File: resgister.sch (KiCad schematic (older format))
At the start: 6 parts, among them U11 74LS245, U12 74LS173, U13 74LS173, U14 74LS245, U15 74LS173, U16 74LS173

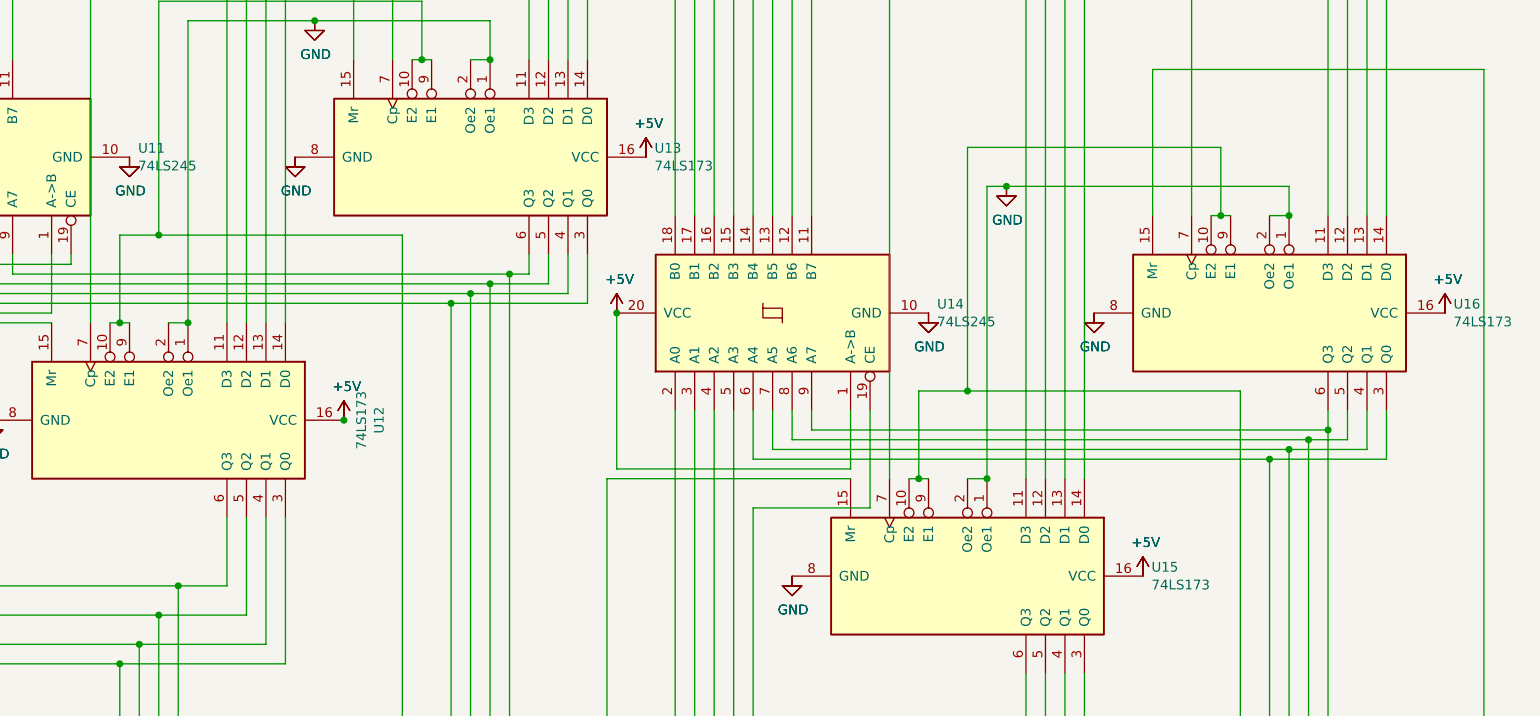
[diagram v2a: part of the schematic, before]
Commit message: Added footprints
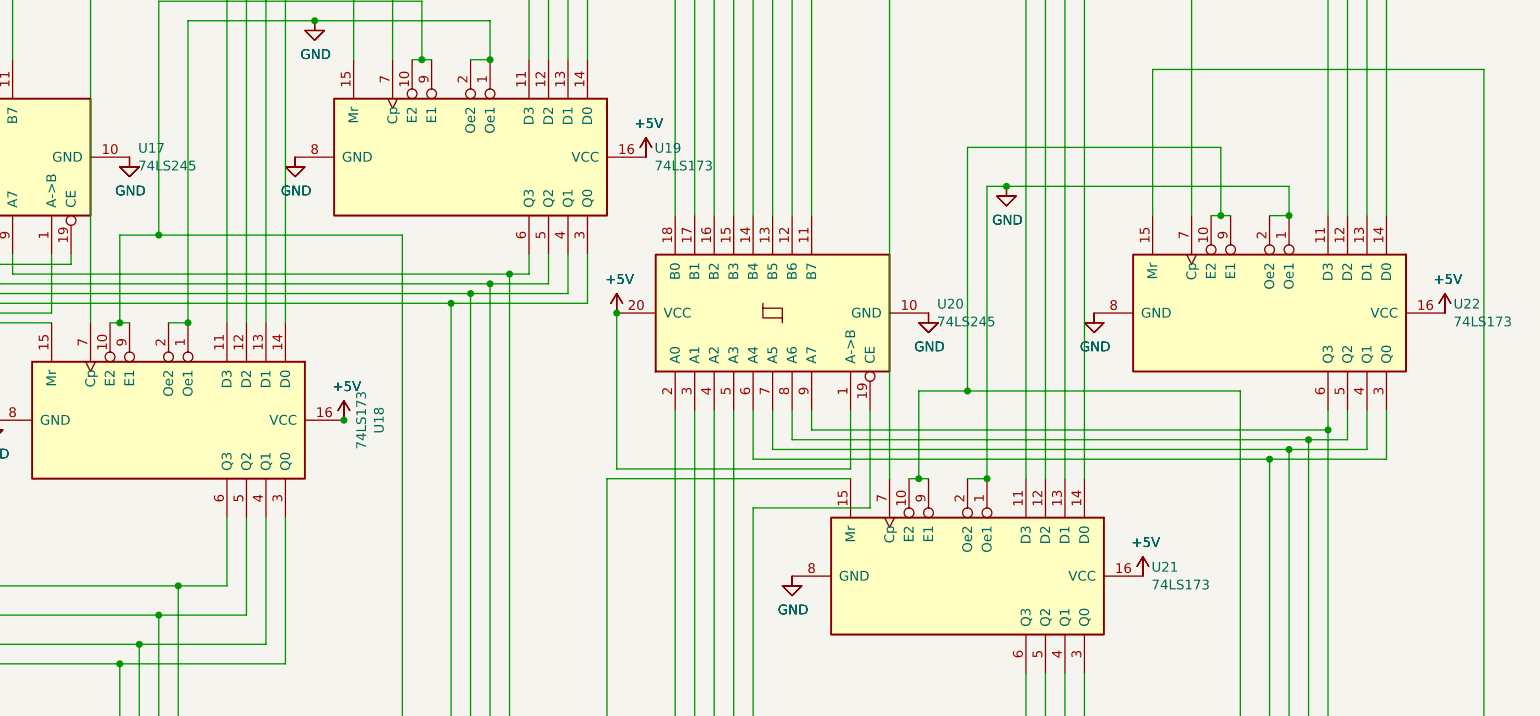
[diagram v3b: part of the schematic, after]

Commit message: Fixed ZIF
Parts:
- U11, U14: symbol 74xx:74LS245 -> 16bitCpu-rescue:74LS245-74xx
- U12, U13, U15, U16: symbol 74xx:74LS173 -> 16bitCpu-rescue:74LS173-74xx
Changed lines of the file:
@@
 	8100 6150 8100 6800
 $Comp
-L power:GND #PWR?
+L 16bitCpu-rescue:GND-power #PWR?
 U 1 1 5F7355A1
 P 7400 4300
@@
 $EndComp
 $Comp
-L power:GND #PWR?
+L 16bitCpu-rescue:GND-power #PWR?
 U 1 1 5F7355A2
 P 8250 4300
@@
 $EndComp
 $Comp
-L power:GND #PWR?
+L 16bitCpu-rescue:GND-power #PWR?
 U 1 1 5F7355A3
 P 6700 5650
@@
 $EndComp
 $Comp
-L power:GND #PWR?
+L 16bitCpu-rescue:GND-power #PWR?
 U 1 1 5F6AAC3B
 P 2600 4850
@@
 $EndComp
 $Comp
-L power:GND #PWR?
+L 16bitCpu-rescue:GND-power #PWR?
 U 1 1 5F6AAC41
 P 3300 3500
@@
 $EndComp
 $Comp
-L power:GND #PWR?
+L 16bitCpu-rescue:GND-power #PWR?
 U 1 1 5F6AAC47
 P 4150 3500
@@
 $EndComp
 $Comp
-L power:+5V #PWR?
+L 16bitCpu-rescue:+5V-power #PWR?
 U 1 1 5F7355A8
 P 4400 4850
@@
 $EndComp
 $Comp
-L power:+5V #PWR?
+L 16bitCpu-rescue:+5V-power #PWR?
 U 1 1 5F7355A9
 P 5800 4300
@@
 $EndComp
 $Comp
-L power:+5V #PWR?
+L 16bitCpu-rescue:+5V-power #PWR?
 U 1 1 5F7355AA
 P 8500 5650
@@
 $EndComp
 $Comp
-L power:+5V #PWR?
+L 16bitCpu-rescue:+5V-power #PWR?
 U 1 1 5F7355AB
 P 10050 4300
@@
 $EndComp
 $Comp
-L power:+5V #PWR?
+L 16bitCpu-rescue:+5V-power #PWR?
 U 1 1 5F7355AC
 P 5950 3500
@@
 Connection ~ 5150 3000
 $Comp
-L power:GND #PWR?
+L 16bitCpu-rescue:GND-power #PWR?
 U 1 1 5F7355AD
 P 4250 2800
@@
 Connection ~ 9250 3800
 $Comp
-L power:GND #PWR?
+L 16bitCpu-rescue:GND-power #PWR?
 U 1 1 5F6AAC87
 P 7800 3650
@@
 	6500 8600 10200 8600
 $Comp
-L 74xx:74LS173 U?
+L 16bitCpu-rescue:74LS173-74xx U?
 U 1 1 5F6AAB55
 P 3500 4850
@@
 $EndComp
 $Comp
-L 74xx:74LS245 U?
+L 16bitCpu-rescue:74LS245-74xx U?
 U 1 1 5F6AAB61
 P 2500 3500
@@
 $EndComp
 $Comp
-L 74xx:74LS173 U?
+L 16bitCpu-rescue:74LS173-74xx U?
 U 1 1 5F73559F
 P 9150 4300
@@
 $EndComp
 $Comp
-L power:GND #PWR?
+L 16bitCpu-rescue:GND-power #PWR?
 U 1 1 5F6AAC29
 P 7400 4300
@@
 $EndComp
 $Comp
-L power:GND #PWR?
+L 16bitCpu-rescue:GND-power #PWR?
 U 1 1 5F6AAC2F
 P 8250 4300
@@
 $EndComp
 $Comp
-L power:GND #PWR?
+L 16bitCpu-rescue:GND-power #PWR?
 U 1 1 5F6AAC35
 P 6700 5650
@@
 $EndComp
 $Comp
-L power:GND #PWR?
+L 16bitCpu-rescue:GND-power #PWR?
 U 1 1 5F7355A4
 P 2600 4850
@@
 $EndComp
 $Comp
-L power:GND #PWR?
+L 16bitCpu-rescue:GND-power #PWR?
 U 1 1 5F7355A5
 P 3300 3500
@@
 $EndComp
 $Comp
-L power:GND #PWR?
+L 16bitCpu-rescue:GND-power #PWR?
 U 1 1 5F7355A6
 P 4150 3500
@@
 $EndComp
 $Comp
-L power:+5V #PWR?
+L 16bitCpu-rescue:+5V-power #PWR?
 U 1 1 5F6AAC4D
 P 1700 3500
@@
 $EndComp
 $Comp
-L power:+5V #PWR?
+L 16bitCpu-rescue:+5V-power #PWR?
 U 1 1 5F6AAC53
 P 4400 4850
@@
 $EndComp
 $Comp
-L power:+5V #PWR?
+L 16bitCpu-rescue:+5V-power #PWR?
 U 1 1 5F6AAC59
 P 5800 4300
@@
 $EndComp
 $Comp
-L power:+5V #PWR?
+L 16bitCpu-rescue:+5V-power #PWR?
 U 1 1 5F6AAC5F
 P 8500 5650
@@
 $EndComp
 $Comp
-L power:+5V #PWR?
+L 16bitCpu-rescue:+5V-power #PWR?
 U 1 1 5F6AAC65
 P 10050 4300
@@
 $EndComp
 $Comp
-L power:+5V #PWR?
+L 16bitCpu-rescue:+5V-power #PWR?
 U 1 1 5F6AAC6B
 P 5950 3500
@@
 $EndComp
 $Comp
-L power:GND #PWR?
+L 16bitCpu-rescue:GND-power #PWR?
 U 1 1 5F6AAC78
 P 4250 2800
@@
 $EndComp
 $Comp
-L power:GND #PWR?
+L 16bitCpu-rescue:GND-power #PWR?
 U 1 1 5F7355AE
 P 7800 3650
@@
 	10250 3050 10250 7750
 $Comp
-L 74xx:74LS173 U?
+L 16bitCpu-rescue:74LS173-74xx U?
 U 1 1 5F6AABCF
 P 7600 5650
@@
 $EndComp
 $Comp
-L 74xx:74LS173 U?
+L 16bitCpu-rescue:74LS173-74xx U?
 U 1 1 5F73559C
 P 5050 3500
@@
 	4700 3900 4700 8100
 $Comp
-L 74xx:74LS245 U?
+L 16bitCpu-rescue:74LS245-74xx U?
 U 1 1 5F7355A0
 P 6600 4300
@@
 Connection ~ 9450 4900
 $Comp
-L power:+5V #PWR?
+L 16bitCpu-rescue:+5V-power #PWR?
 U 1 1 5F7355A7
 P 1700 3500

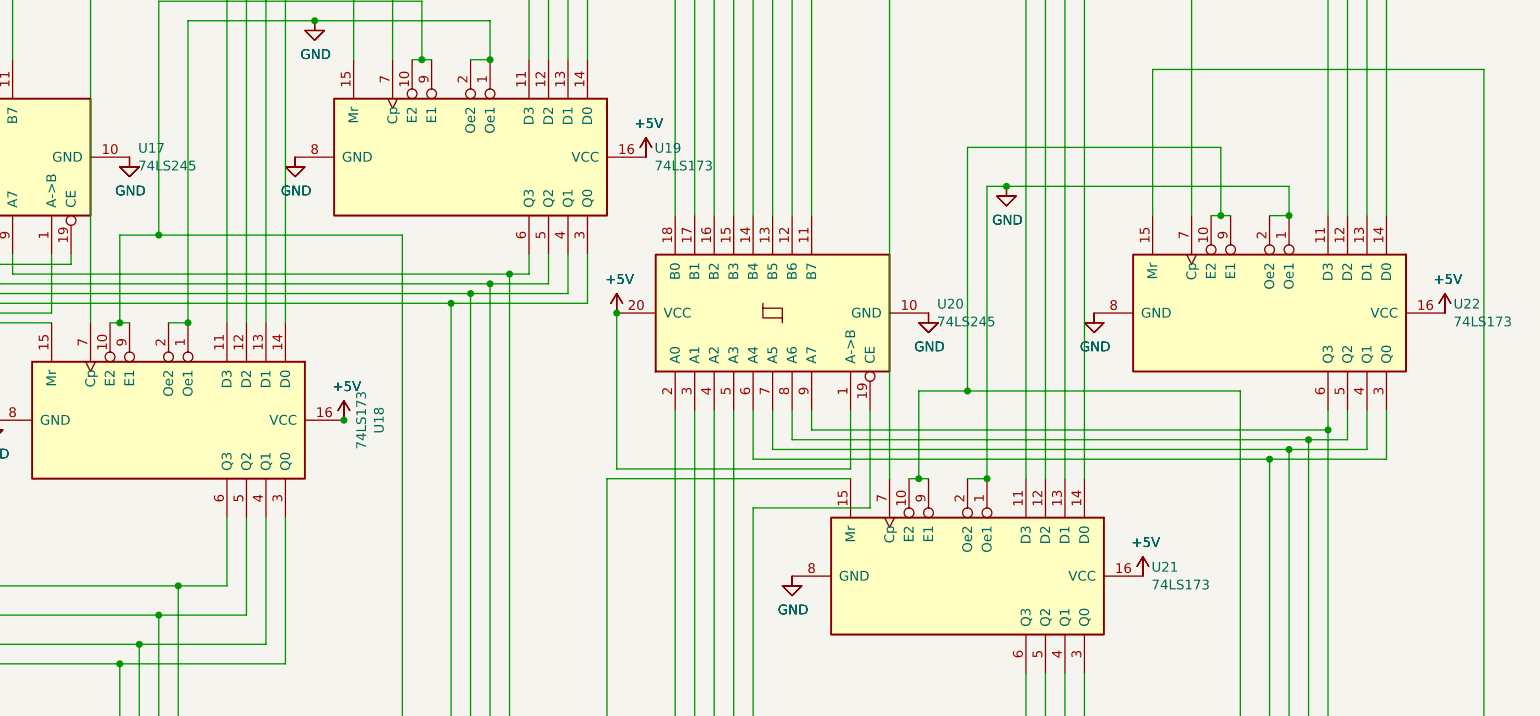
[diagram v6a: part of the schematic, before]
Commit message: Added GND and PWR in ALU and removed the Error
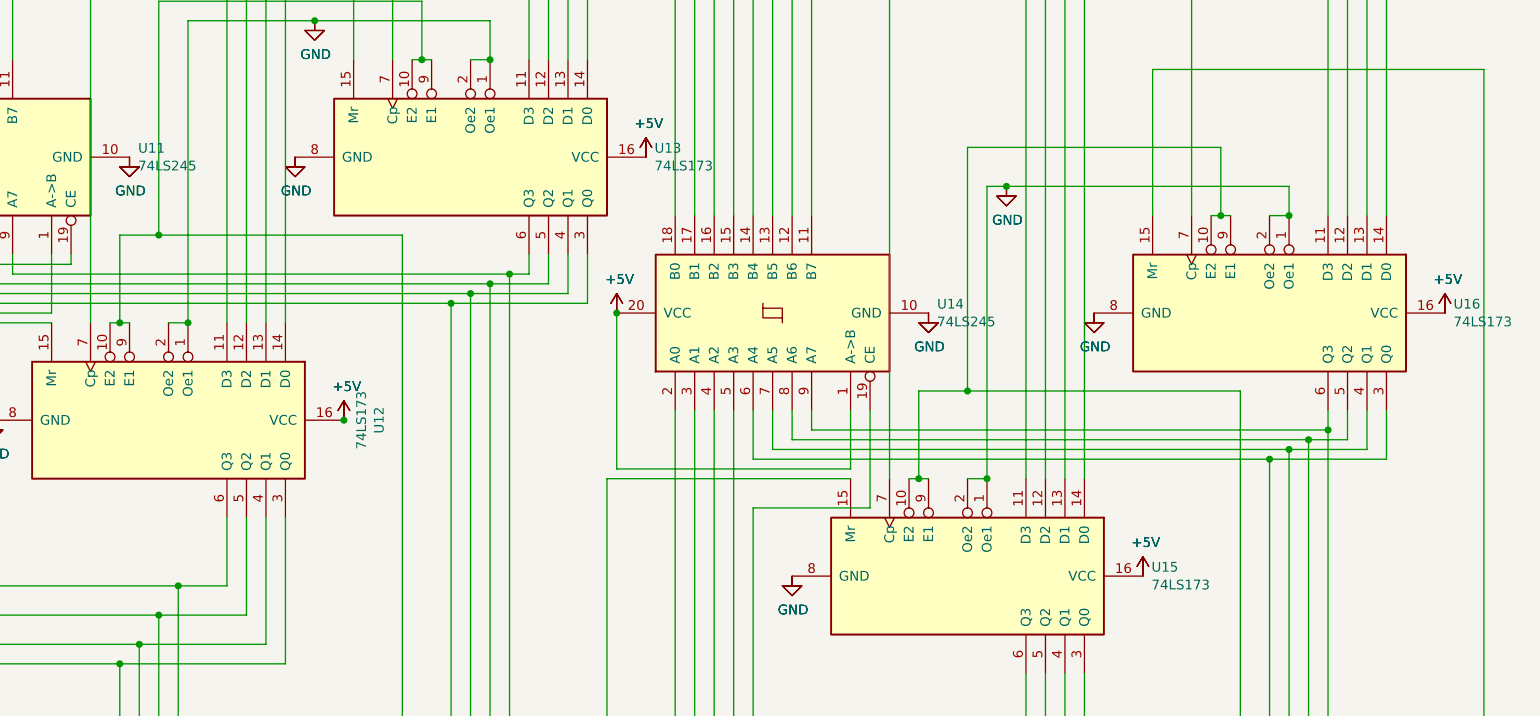
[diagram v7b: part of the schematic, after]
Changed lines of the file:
@@
 $Descr A3 16535 11693
 encoding utf-8
-Sheet 4 9
+Sheet 3 9
 Title ""
 Date ""
@@
 AR Path="/603B766D/5F6AAB55" Ref="U?"  Part="1"
 AR Path="/5F74778C/5F6AAB55" Ref="U18"  Part="1"
-F 0 "U18" H 3500 5931 50  0000 C CNN
+F 0 "U12" H 3500 5931 50  0000 C CNN
 F 1 "74LS173" H 3500 5840 50  0000 C CNN
 F 2 "Package_DIP:DIP-16_W7.62mm" H 3500 4850 50  0001 C CNN
@@
 AR Path="/603B766D/5F6AAB61" Ref="U?"  Part="1"
 AR Path="/5F74778C/5F6AAB61" Ref="U17"  Part="1"
-F 0 "U17" V 2546 2656 50  0000 R CNN
+F 0 "U11" V 2546 2656 50  0000 R CNN
 F 1 "74LS245" V 2455 2656 50  0000 R CNN
 F 2 "Package_DIP:DIP-20_W7.62mm" H 2500 3500 50  0001 C CNN
@@
 AR Path="/603B766D/5F73559F" Ref="U?"  Part="1"
 AR Path="/5F74778C/5F73559F" Ref="U22"  Part="1"
-F 0 "U22" V 9104 5244 50  0000 L CNN
+F 0 "U16" V 9104 5244 50  0000 L CNN
 F 1 "74LS173" V 9195 5244 50  0000 L CNN
 F 2 "Package_DIP:DIP-16_W7.62mm" H 9150 4300 50  0001 C CNN
@@
 AR Path="/603B766D/5F6AABCF" Ref="U?"  Part="1"
 AR Path="/5F74778C/5F6AABCF" Ref="U21"  Part="1"
-F 0 "U21" V 7554 6594 50  0000 L CNN
+F 0 "U15" V 7554 6594 50  0000 L CNN
 F 1 "74LS173" V 7645 6594 50  0000 L CNN
 F 2 "Package_DIP:DIP-16_W7.62mm" H 7600 5650 50  0001 C CNN
@@
 AR Path="/603B766D/5F73559C" Ref="U?"  Part="1"
 AR Path="/5F74778C/5F73559C" Ref="U19"  Part="1"
-F 0 "U19" V 5004 4444 50  0000 L CNN
+F 0 "U13" V 5004 4444 50  0000 L CNN
 F 1 "74LS173" V 5095 4444 50  0000 L CNN
 F 2 "Package_DIP:DIP-16_W7.62mm" H 5050 3500 50  0001 C CNN
@@
 AR Path="/603B766D/5F7355A0" Ref="U?"  Part="1"
 AR Path="/5F74778C/5F7355A0" Ref="U20"  Part="1"
-F 0 "U20" V 6646 3456 50  0000 R CNN
+F 0 "U14" V 6646 3456 50  0000 R CNN
 F 1 "74LS245" V 6555 3456 50  0000 R CNN
 F 2 "Package_DIP:DIP-20_W7.62mm" H 6600 4300 50  0001 C CNN

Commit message: made the CU , need to change the IR
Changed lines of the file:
@@
 AR Path="/603B766D/5F6AAB55" Ref="U?"  Part="1"
 AR Path="/5F74778C/5F6AAB55" Ref="U18"  Part="1"
-F 0 "U12" H 3500 5931 50  0000 C CNN
+F 0 "U18" H 3500 5931 50  0000 C CNN
 F 1 "74LS173" H 3500 5840 50  0000 C CNN
 F 2 "Package_DIP:DIP-16_W7.62mm" H 3500 4850 50  0001 C CNN
@@
 AR Path="/603B766D/5F6AAB61" Ref="U?"  Part="1"
 AR Path="/5F74778C/5F6AAB61" Ref="U17"  Part="1"
-F 0 "U11" V 2546 2656 50  0000 R CNN
+F 0 "U17" V 2546 2656 50  0000 R CNN
 F 1 "74LS245" V 2455 2656 50  0000 R CNN
 F 2 "Package_DIP:DIP-20_W7.62mm" H 2500 3500 50  0001 C CNN
@@
 AR Path="/603B766D/5F73559F" Ref="U?"  Part="1"
 AR Path="/5F74778C/5F73559F" Ref="U22"  Part="1"
-F 0 "U16" V 9104 5244 50  0000 L CNN
+F 0 "U22" V 9104 5244 50  0000 L CNN
 F 1 "74LS173" V 9195 5244 50  0000 L CNN
 F 2 "Package_DIP:DIP-16_W7.62mm" H 9150 4300 50  0001 C CNN
@@
 AR Path="/603B766D/5F6AABCF" Ref="U?"  Part="1"
 AR Path="/5F74778C/5F6AABCF" Ref="U21"  Part="1"
-F 0 "U15" V 7554 6594 50  0000 L CNN
+F 0 "U21" V 7554 6594 50  0000 L CNN
 F 1 "74LS173" V 7645 6594 50  0000 L CNN
 F 2 "Package_DIP:DIP-16_W7.62mm" H 7600 5650 50  0001 C CNN
@@
 AR Path="/603B766D/5F73559C" Ref="U?"  Part="1"
 AR Path="/5F74778C/5F73559C" Ref="U19"  Part="1"
-F 0 "U13" V 5004 4444 50  0000 L CNN
+F 0 "U19" V 5004 4444 50  0000 L CNN
 F 1 "74LS173" V 5095 4444 50  0000 L CNN
 F 2 "Package_DIP:DIP-16_W7.62mm" H 5050 3500 50  0001 C CNN
@@
 AR Path="/603B766D/5F7355A0" Ref="U?"  Part="1"
 AR Path="/5F74778C/5F7355A0" Ref="U20"  Part="1"
-F 0 "U14" V 6646 3456 50  0000 R CNN
+F 0 "U20" V 6646 3456 50  0000 R CNN
 F 1 "74LS245" V 6555 3456 50  0000 R CNN
 F 2 "Package_DIP:DIP-20_W7.62mm" H 6600 4300 50  0001 C CNN
